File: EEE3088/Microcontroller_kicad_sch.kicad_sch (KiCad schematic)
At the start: 12 parts, among them J2 Conn_01x24, J3 Conn_01x24

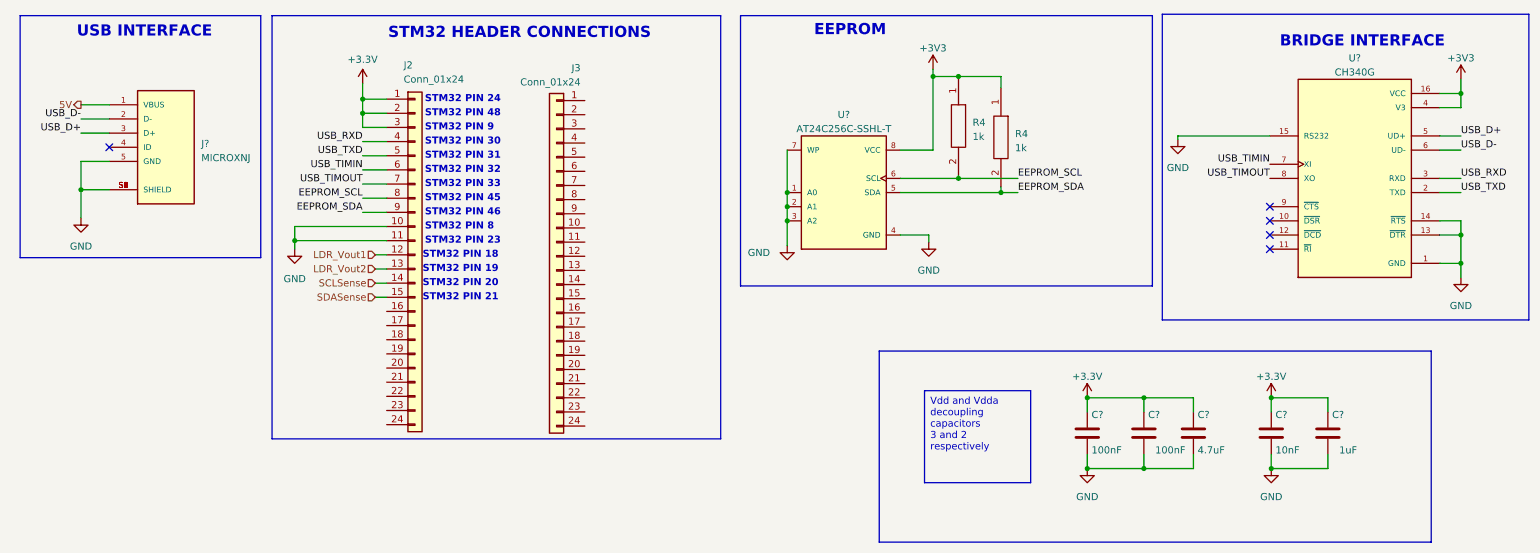
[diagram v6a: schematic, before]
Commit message: Added test points & 0 Ohm
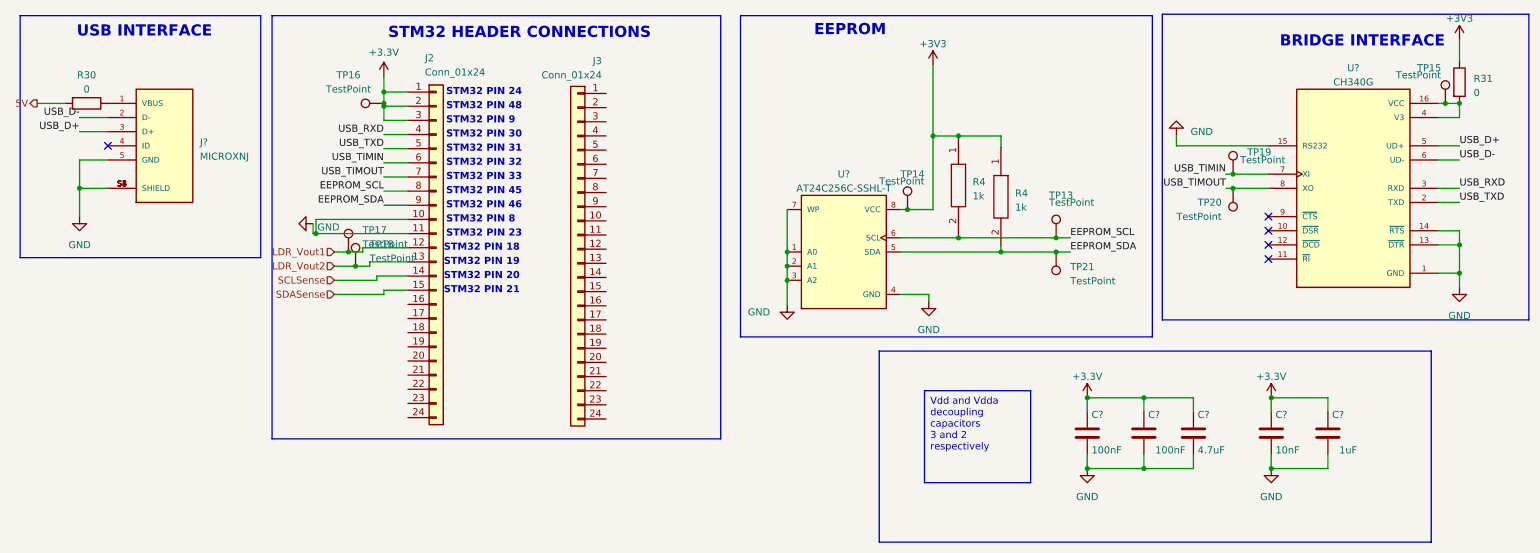
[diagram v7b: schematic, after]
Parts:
- added R30, R31: 0, RESC1005X40N, symbol Device:R
- added TP13, TP14, TP15, TP16, TP17, TP18, TP19, TP20, TP21: TestPoint, symbol Connector:TestPoint
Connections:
- net +3.3V: now also TP16.1
- net +3V3: now also R31.1, TP14.1; no longer U?.16 (VCC), U?.4 (V3)
- net 5V: now also R30.2; no longer J?.1 (VBUS)
- net EEPROM_SCL: now also TP13.1
- net EEPROM_SDA: now also TP21.1
- net LDR_Vout1: now also TP17.1
- net LDR_Vout2: now also TP18.1
- net USB_TIMIN: now also TP19.1
- net USB_TIMOUT: now also TP20.1
- new net: R31.2, TP15.1, U?.16 (VCC), U?.4 (V3)
- new net: J?.1 (VBUS), R30.1
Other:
- moved on the sheet: J2, J3, R4, U?

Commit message: power
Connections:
- net 5V renamed +5V
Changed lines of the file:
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@@
-    (effects (font (size 1.27 1.27)) (justify right))
-  )
-  (hierarchical_label "5V" (shape output) (at 15.24 33.02 180) (fields_autoplaced)
     (effects (font (size 1.27 1.27)) (justify right))
   )
@@
         )
       )
+    )
+  )
+  (symbol (lib_id "power:+5V") (at 15.24 33.02 0) (unit 1)
+    (in_bom yes) (on_board yes) (dnp no) (fields_autoplaced)
+    (property "Reference" "#PWR046" (at 15.24 36.83 0)
+      (effects (font (size 1.27 1.27)) hide)
+    )
+    (property "Value" "+5V" (at 15.24 29.21 0)
+      (effects (font (size 1.27 1.27)))
+    )
+    (property "Footprint" "" (at 15.24 33.02 0)
+      (effects (font (size 1.27 1.27)) hide)
+    )
+    (property "Datasheet" "" (at 15.24 33.02 0)
+      (effects (font (size 1.27 1.27)) hide)
+    )
+    (pin "1")
+    (instances
+      (project "EEE3088"
+        (path "/83bdd5e1-981a-4ca1-9a2f-70dea9f00850/af4ae736-8069-4035-bb69-27168d826fe0"
+          (reference "#PWR046") (unit 1)
+        )
+      )
